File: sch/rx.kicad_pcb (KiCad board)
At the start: 2 copper layers, 48 x 70 mm, 49 parts, among them K1 CONN_3, K2 CONN_3, P1 FromBPF, P2 CONN_2, P3 CONN_4, T1 COILCRAFT_WBC-B, U1 LP2992AIM5-5.0V, U2 SN65LVDS2DBV, U3 SN65LVDS2DBV, U4 LP2992AIM5-3.3V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

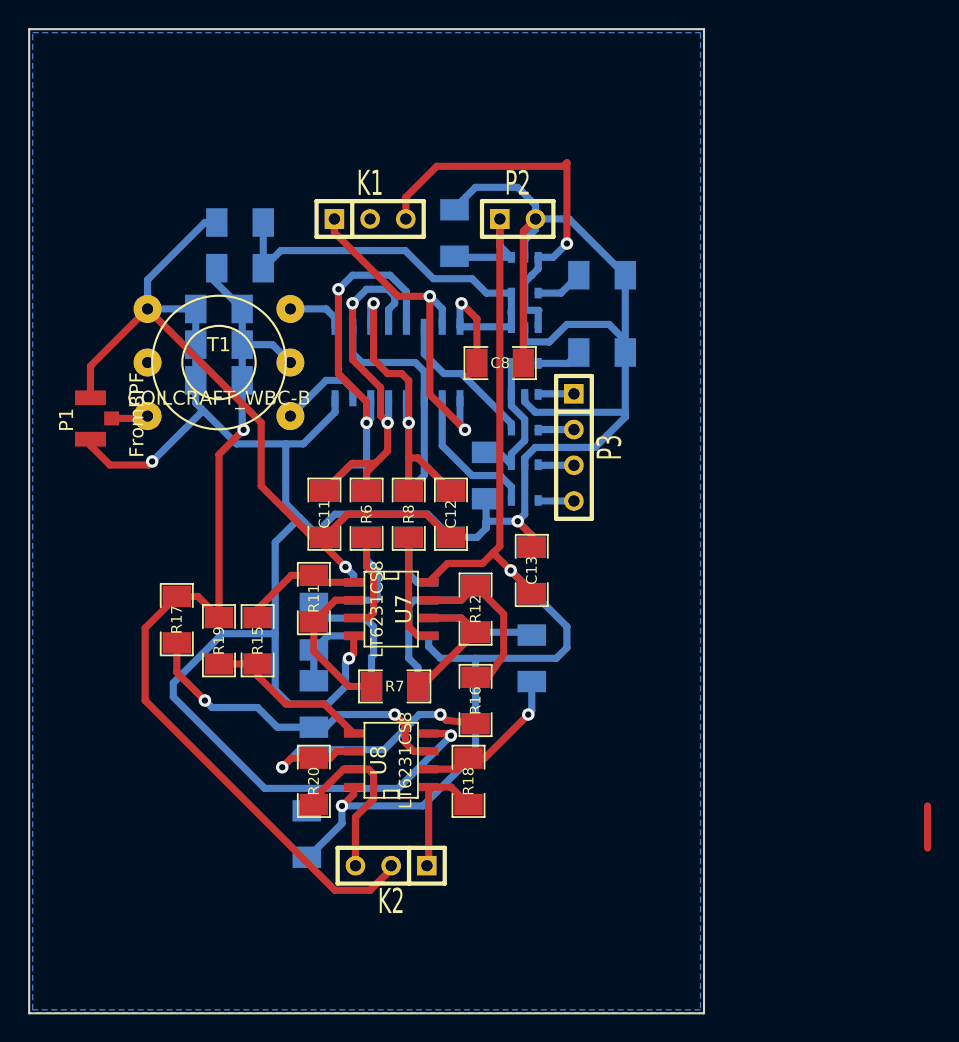
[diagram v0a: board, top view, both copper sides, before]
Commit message: Fill more board space with ground in RX
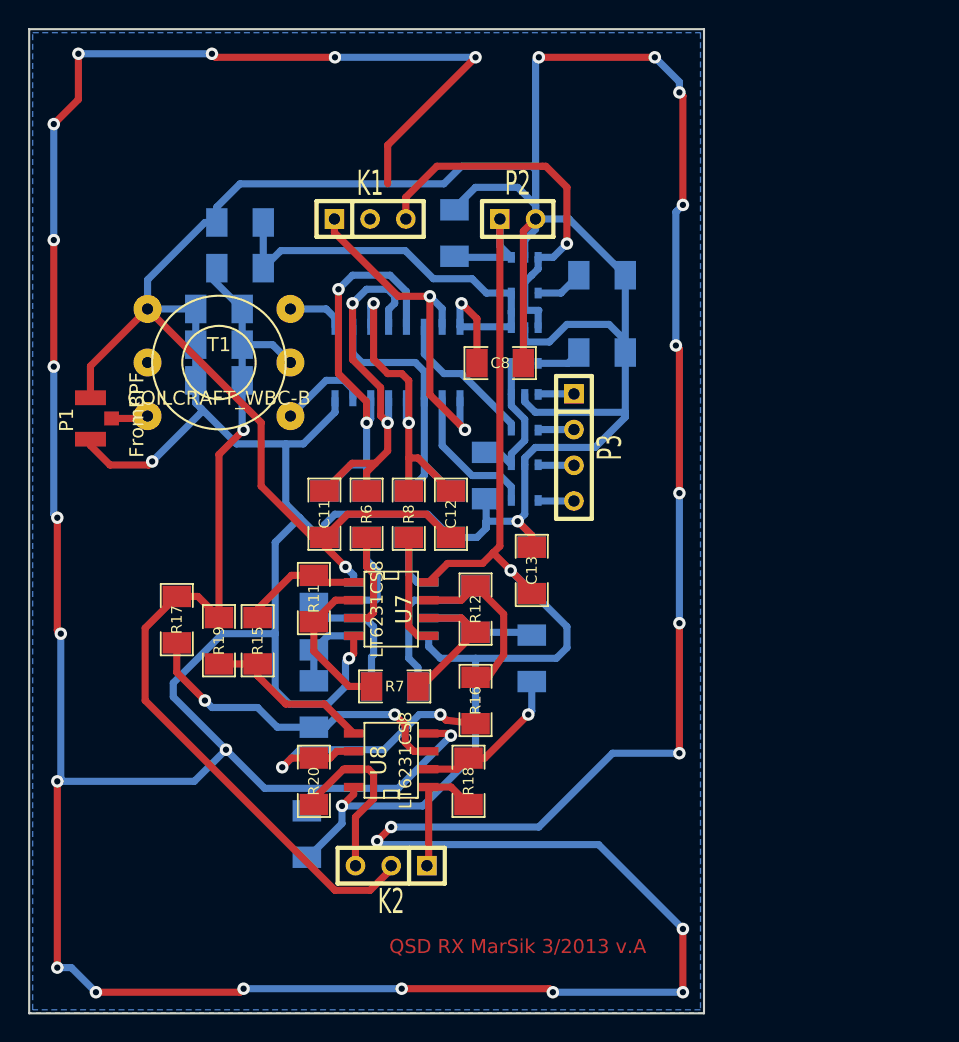
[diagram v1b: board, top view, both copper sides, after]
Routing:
- net GND: track 249.1 -> 565.4 mm, vias 5 -> 33
- net (no net): track 3.00 -> 0.00 mm
- net N-0000038: track 28.6 -> 27.4 mm
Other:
- board text added: "QSD RX MarSik 3/2013 v.A"
